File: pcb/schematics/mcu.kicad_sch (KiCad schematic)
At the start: 1 part

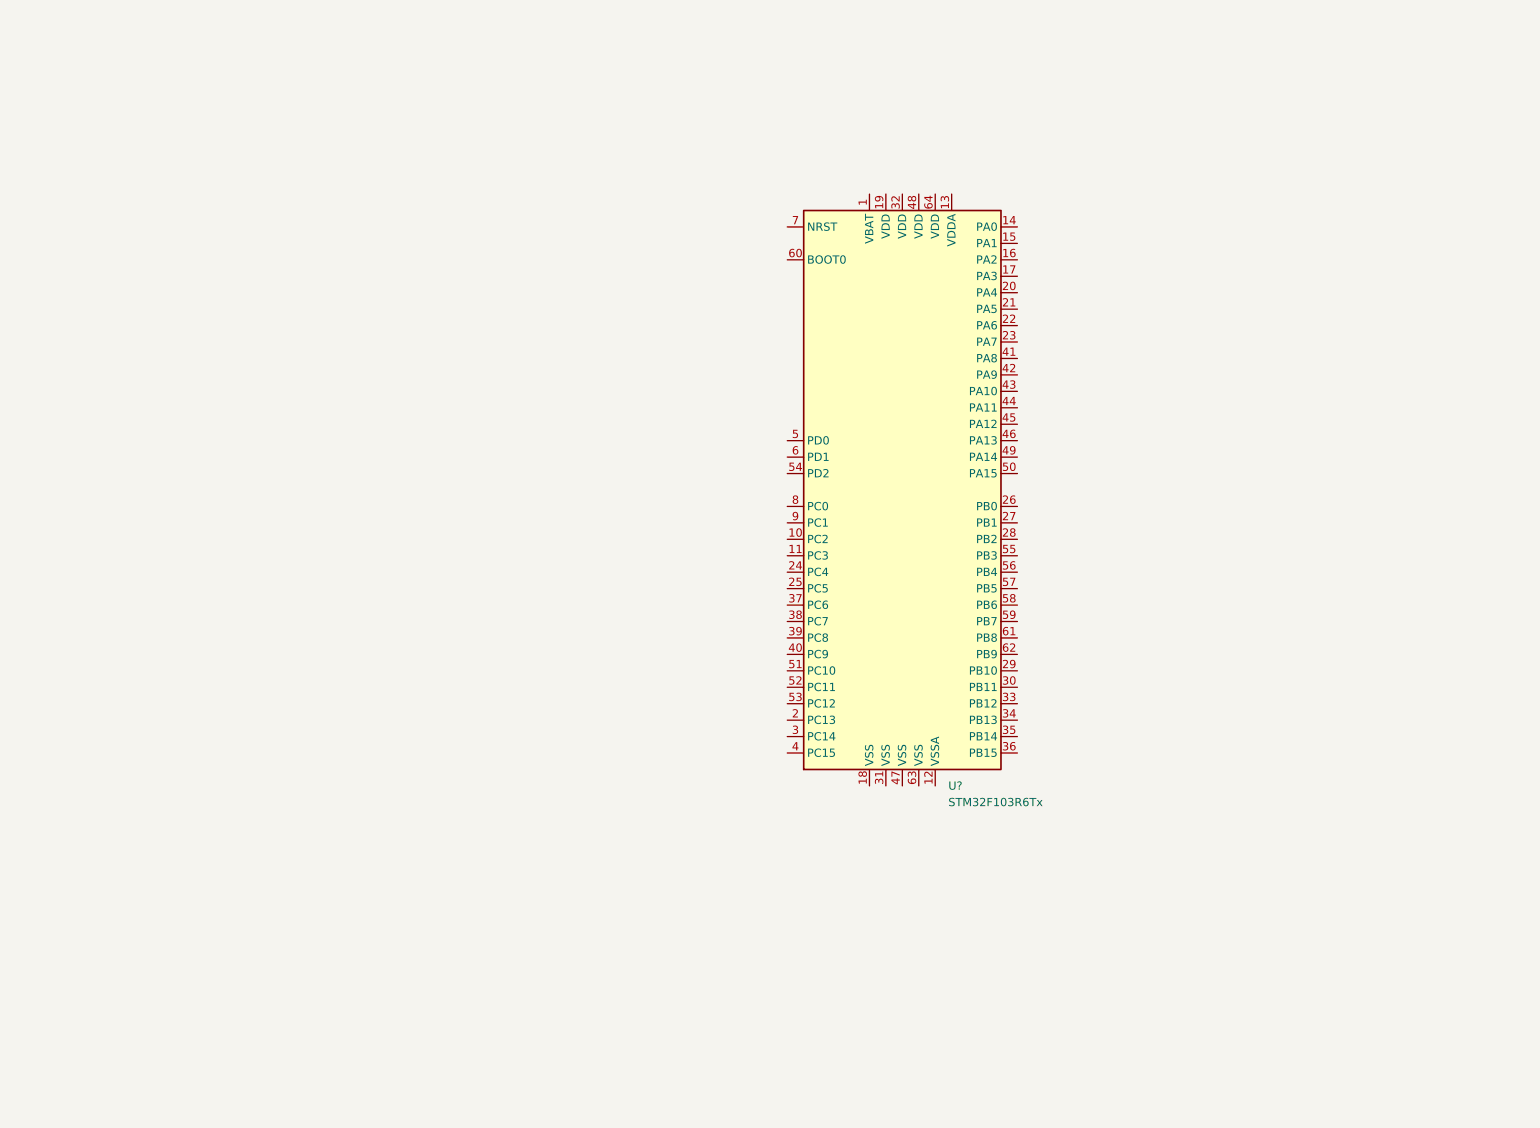
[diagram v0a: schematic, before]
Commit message: start choosing components, need to add overcurren t protection
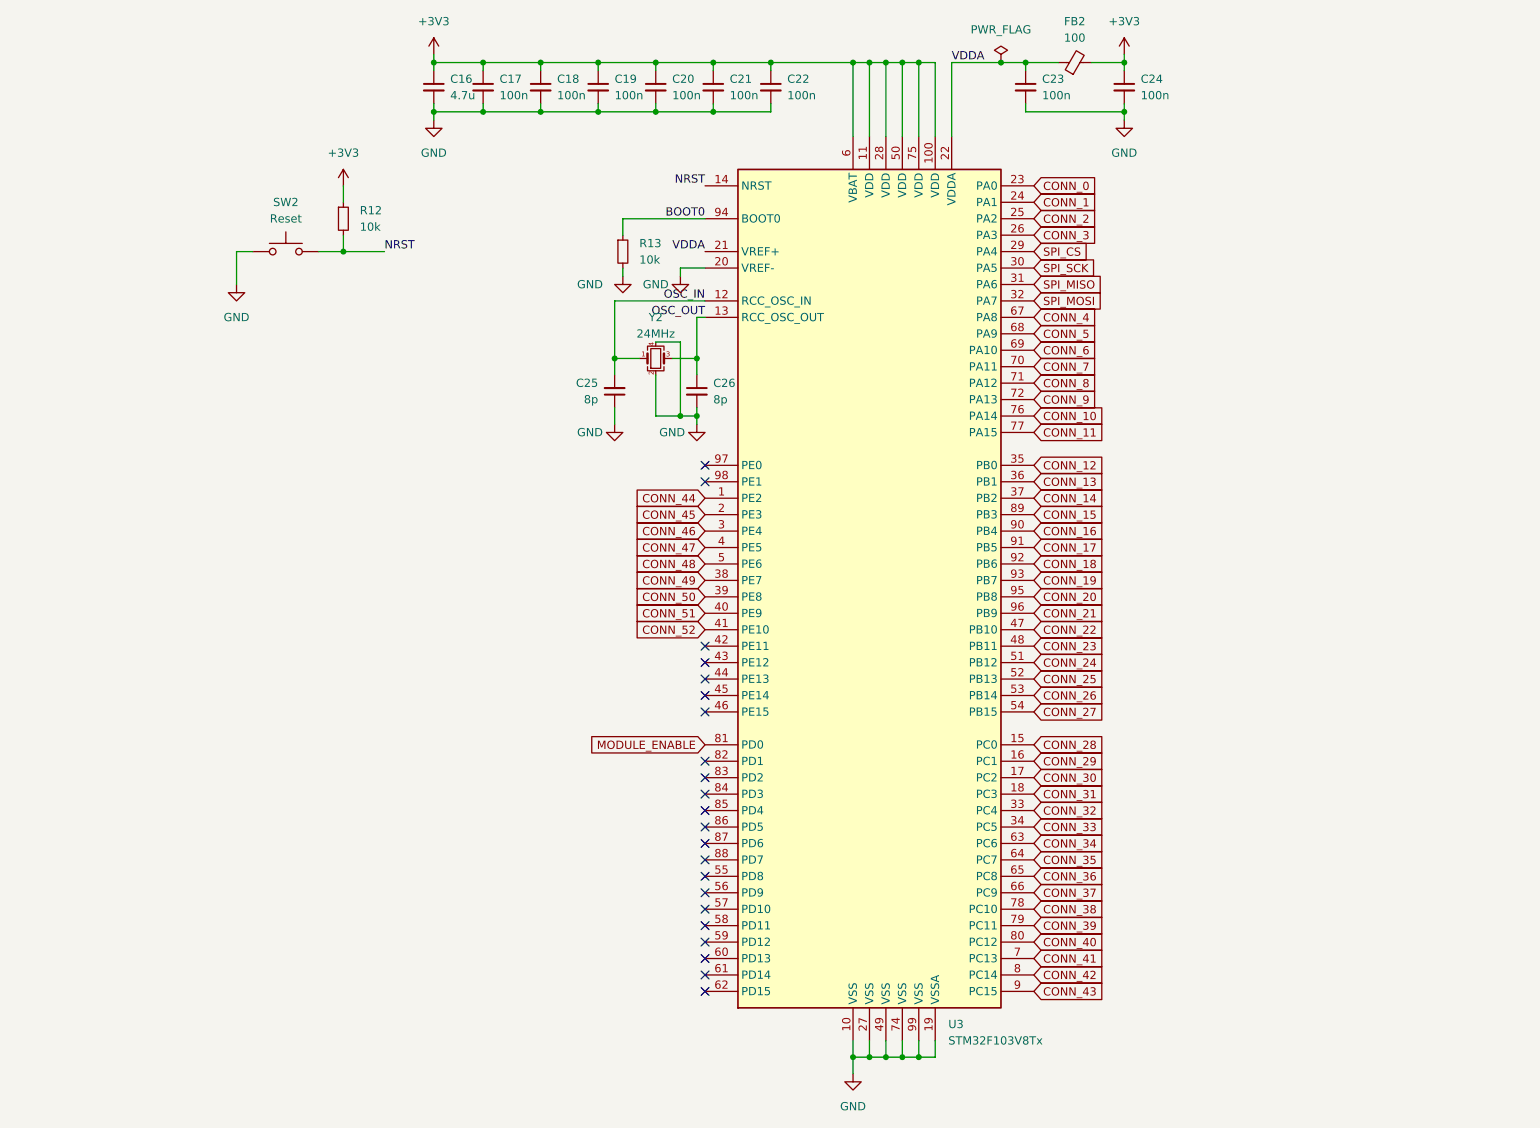
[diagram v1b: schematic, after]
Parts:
- removed U?: STM32F103R6Tx, Package_QFP:LQFP-64_10x10mm_P0.5mm, symbol MCU_ST_STM32F1:STM32F103R6Tx
- added C16: 4.7u, Capacitor_SMD:C_0805_2012Metric, symbol Device:C_Small
- added C17, C18, C19, C20, C21, C22, C23, C24: 100n, Capacitor_SMD:C_0603_1608Metric, symbol Device:C_Small
- added C25, C26: 8p, Capacitor_SMD:C_0603_1608Metric, symbol Device:C_Small
- added FB2: 100, symbol Device:FerriteBead_Small
- added R12, R13: 10k, symbol Device:R_Small
- added SW2: Reset, symbol Switch:SW_Push
- added U3: STM32F103V8Tx, Package_QFP:LQFP-100_14x14mm_P0.5mm, symbol MCU_ST_STM32F1:STM32F103V8Tx
- added Y2: 24MHz, Crystal:Crystal_SMD_SeikoEpson_TSX3225-4Pin_3.2x2.5mm, symbol Device:Crystal_GND24_Small
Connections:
- new net +3V3: C16.1, C17.1, C18.1, C19.1, C20.1, C21.1, C22.1, C24.1, FB2.2, R12.1, U3.100 (VDD), U3.11 (VDD), U3.28 (VDD), U3.50 (VDD), U3.6 (VBAT), U3.75 (VDD)
- new net BOOT0: R13.1, U3.94 (BOOT0)
- new net CONN_0: U3.23 (PA0)
- new net CONN_1: U3.24 (PA1)
- new net CONN_10: U3.76 (PA14)
- new net CONN_11: U3.77 (PA15)
- new net CONN_12: U3.35 (PB0)
- new net CONN_13: U3.36 (PB1)
- new net CONN_14: U3.37 (PB2)
- new net CONN_15: U3.89 (PB3)
- new net CONN_16: U3.90 (PB4)
- new net CONN_17: U3.91 (PB5)
- new net CONN_18: U3.92 (PB6)
- new net CONN_19: U3.93 (PB7)
- new net CONN_2: U3.25 (PA2)
- new net CONN_20: U3.95 (PB8)
- new net CONN_21: U3.96 (PB9)
- new net CONN_22: U3.47 (PB10)
- new net CONN_23: U3.48 (PB11)
- new net CONN_24: U3.51 (PB12)
- new net CONN_25: U3.52 (PB13)
- new net CONN_26: U3.53 (PB14)
- new net CONN_27: U3.54 (PB15)
- new net CONN_28: U3.15 (PC0)
- new net CONN_29: U3.16 (PC1)
- new net CONN_3: U3.26 (PA3)
- new net CONN_30: U3.17 (PC2)
- new net CONN_31: U3.18 (PC3)
- new net CONN_32: U3.33 (PC4)
- new net CONN_33: U3.34 (PC5)
- new net CONN_34: U3.63 (PC6)
- new net CONN_35: U3.64 (PC7)
- new net CONN_36: U3.65 (PC8)
- new net CONN_37: U3.66 (PC9)
- new net CONN_38: U3.78 (PC10)
- new net CONN_39: U3.79 (PC11)
- new net CONN_4: U3.67 (PA8)
- new net CONN_40: U3.80 (PC12)
- new net CONN_41: U3.7 (PC13)
- new net CONN_42: U3.8 (PC14)
- new net CONN_43: U3.9 (PC15)
- new net CONN_44: U3.1 (PE2)
- new net CONN_45: U3.2 (PE3)
- new net CONN_46: U3.3 (PE4)
- new net CONN_47: U3.4 (PE5)
- new net CONN_48: U3.5 (PE6)
- new net CONN_49: U3.38 (PE7)
- new net CONN_5: U3.68 (PA9)
- new net CONN_50: U3.39 (PE8)
- new net CONN_51: U3.40 (PE9)
- new net CONN_52: U3.41 (PE10)
- new net CONN_6: U3.69 (PA10)
- new net CONN_7: U3.70 (PA11)
- new net CONN_8: U3.71 (PA12)
- new net CONN_9: U3.72 (PA13)
- new net GND: C16.2, C17.2, C18.2, C19.2, C20.2, C21.2, C22.2, C23.2, C24.2, C25.1, C26.2, R13.2, SW2.1, U3.10 (VSS), U3.19 (VSSA), U3.20 (VREF-), U3.27 (VSS), U3.49 (VSS), U3.74 (VSS), U3.99 (VSS), Y2.2, Y2.4
- new net MODULE_ENABLE: U3.81 (PD0)
- new net NRST: R12.2, SW2.2, U3.14 (NRST)
- new net OSC_IN: C25.2, U3.12 (RCC_OSC_IN), Y2.1
- new net OSC_OUT: C26.1, U3.13 (RCC_OSC_OUT), Y2.3
- new net SPI_CS: U3.29 (PA4)
- new net SPI_MISO: U3.31 (PA6)
- new net SPI_MOSI: U3.32 (PA7)
- new net SPI_SCK: U3.30 (PA5)
- new net VDDA: C23.1, FB2.1, U3.21 (VREF+), U3.22 (VDDA)
- no-connect marks 0 -> 22

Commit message: add current sensing
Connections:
- net NRST renamed RESET
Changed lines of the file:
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@@
-    (effects (font (size 1.27 1.27)) (justify right bottom))
-  )
-  (label "NRST" (at 121.92 46.99 180)
     (effects (font (size 1.27 1.27)) (justify right bottom))
   )
@@
   (label "BOOT0" (at 121.92 52.07 180)
     (effects (font (size 1.27 1.27)) (justify right bottom))
-  )
-  (label "NRST" (at 72.39 57.15 0)
-    (effects (font (size 1.27 1.27)) (justify left bottom))
   )
   (label "OSC_OUT" (at 121.92 67.31 180)
@@
     (effects (font (size 1.27 1.27)) (justify left))
     (property "Intersheet References" "${INTERSHEET_REFS}" (id 0) (at 182.5717 54.5306 0)
+      (effects (font (size 1.27 1.27)) (justify left))
+    )
+  )
+  (global_label "RESET" (shape input) (at 72.39 57.15 0) (fields_autoplaced)
+    (effects (font (size 1.27 1.27)) (justify left))
+    (property "Intersheet References" "${INTERSHEET_REFS}" (id 0) (at 80.5483 57.0706 0)
       (effects (font (size 1.27 1.27)) (justify left))
     )
@@
     )
   )
+  (global_label "RESET" (shape input) (at 121.92 46.99 180) (fields_autoplaced)
+    (effects (font (size 1.27 1.27)) (justify right))
+    (property "Intersheet References" "${INTERSHEET_REFS}" (id 0) (at 113.7617 46.9106 0)
+      (effects (font (size 1.27 1.27)) (justify right))
+    )
+  )

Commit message: finish the schematic
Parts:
- FB2: footprint (none) -> Inductor_SMD:L_0805_2012Metric; Part Number (none) -> MG2029-101Y
- R12, R13: footprint (none) -> Resistor_SMD:R_0603_1608Metric; Part Number (none) -> CR0603-FX-1002ELF
- SW2: footprint (none) -> Button_Switch_SMD:Panasonic_EVQPUJ_EVQPUA
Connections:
- net MODULE_RESET: now reaches U3.82 (PD1)
- no-connect marks 22 -> 21
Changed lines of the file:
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@@
   (no_connect (at 121.92 143.51))
   (no_connect (at 121.92 138.43))
-  (no_connect (at 121.92 135.89))
   (no_connect (at 121.92 90.17))
   (no_connect (at 121.92 92.71))
@@
     )
   )
+  (global_label "CURRENT_SENSE" (shape input) (at 87.63 143.51 0) (fields_autoplaced)
+    (effects (font (size 1.27 1.27)) (justify left))
+    (property "Intersheet References" "${INTERSHEET_REFS}" (id 0) (at 105.646 143.4306 0)
+      (effects (font (size 1.27 1.27)) (justify left))
+    )
+  )
   (global_label "CONN_7" (shape input) (at 172.72 74.93 0) (fields_autoplaced)
     (effects (font (size 1.27 1.27)) (justify left))
@@
     )
   )
+  (global_label "MODULE_RESET" (shape input) (at 121.92 135.89 180) (fields_autoplaced)
+    (effects (font (size 1.27 1.27)) (justify right))
+    (property "Intersheet References" "${INTERSHEET_REFS}" (id 0) (at 105.2345 135.8106 0)
+      (effects (font (size 1.27 1.27)) (justify right))
+    )
+  )
   (global_label "CONN_51" (shape input) (at 121.92 113.03 180)
     (effects (font (size 1.27 1.27)) (justify right))
@@
     (property "Reference" "FB2" (id 0) (at 179.0319 21.59 90))
     (property "Value" "100" (id 1) (at 179.0319 24.13 90))
-    (property "Footprint" "" (id 2) (at 179.07 29.718 90)
+    (property "Footprint" "Inductor_SMD:L_0805_2012Metric" (id 2) (at 179.07 29.718 90)
       (effects (font (size 1.27 1.27)) hide)
     )
     (property "Datasheet" "~" (id 3) (at 179.07 27.94 0)
+      (effects (font (size 1.27 1.27)) hide)
+    )
+    (property "Part Number" "MG2029-101Y" (id 4) (at 179.07 27.94 0)
       (effects (font (size 1.27 1.27)) hide)
     )
@@
       (effects (font (size 1.27 1.27)) (justify left))
     )
-    (property "Footprint" "" (id 2) (at 66.04 52.07 0)
+    (property "Footprint" "Resistor_SMD:R_0603_1608Metric" (id 2) (at 66.04 52.07 0)
       (effects (font (size 1.27 1.27)) hide)
     )
@@
       (effects (font (size 1.27 1.27)) hide)
     )
+    (property "Part Number" "CR0603-FX-1002ELF" (id 4) (at 66.04 52.07 0)
+      (effects (font (size 1.27 1.27)) hide)
+    )
     (pin "1")
     (pin "2")
@@
       (effects (font (size 1.27 1.27)) (justify left))
     )
-    (property "Footprint" "" (id 2) (at 109.22 57.15 0)
+    (property "Footprint" "Resistor_SMD:R_0603_1608Metric" (id 2) (at 109.22 57.15 0)
       (effects (font (size 1.27 1.27)) hide)
     )
     (property "Datasheet" "~" (id 3) (at 109.22 57.15 0)
+      (effects (font (size 1.27 1.27)) hide)
+    )
+    (property "Part Number" "CR0603-FX-1002ELF" (id 4) (at 109.22 57.15 0)
       (effects (font (size 1.27 1.27)) hide)
     )
@@
     (property "Reference" "SW2" (id 0) (at 57.15 49.53 0))
     (property "Value" "Reset" (id 1) (at 57.15 52.07 0))
-    (property "Footprint" "" (id 2) (at 57.15 52.07 0)
-      (effects (font (size 1.27 1.27)) hide)
-    )
+    (property "Footprint" "Button_Switch_SMD:Panasonic_EVQPUJ_EVQPUA" (id 2) (at 57.15 52.07 0)
+      (effects (font (size 1.27 1.27)) hide)
+    )
